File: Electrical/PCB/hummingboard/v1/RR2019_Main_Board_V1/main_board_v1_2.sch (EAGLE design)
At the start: 143 parts, among them CN1 MIRCO_B, IC1 OR_SC70-5, J10 I2C_5V_4, J11 SERVO_LEFT, J12 SERVO_RIGHT, J13 ESC, J14 5V_INPUT, J15 QUAD_ENCODER_2, J16 7.2V_INPUT, J17 I2C_5V_FXIO_1, J18 I2C_5V_FXIO_2, J19 JETSON_TRIGGER, J2 REAR_ENCODER, J20 QUAD_ENCODER_1, J21 BLDC_HALL, J22 SPI_FXIO_1, J3 FRONT_ENCODER, J4 I2C_1V8_1, J5 SPI_2, J6 WIRELESS_MODULE, J7 UART_0, J8 UART_2, J9 STEERING_ANGLE, Q1 BSS138, Q3 DMP2066LSN, Q4 BSS138, Q5 BSS138, Q6 BSS138, Q7 BSS138, Q8 BSS138, U3 ICM-20948, U4 PCA9306

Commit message: layout complete v.1
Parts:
- added JP12: POWER2, adafruit:PINHD-1X3
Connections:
- net +1.8V: now also JP6.4; no longer JP6.5
- net +3V3: now also JP12.1, JP12.2; no longer JP6.4
- net GND: now also JP12.3, JP6.5
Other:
- moved on the sheet: JP6
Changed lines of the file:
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@@
 <part name="U$46" library="RobotRacing2019_Master" deviceset="+VDD" device=""/>
 <part name="JP6" library="adafruit" library_urn="urn:adsk.eagle:library:420" deviceset="PINHD-1X8" device="BIG" package3d_urn="urn:adsk.eagle:package:6240707/1" value="POWER"/>
-<part name="U$47" library="RobotRacing2019_Master" deviceset="+3V3" device=""/>
 <part name="JP7" library="adafruit" library_urn="urn:adsk.eagle:library:420" deviceset="PINHD-1X3" device="" package3d_urn="urn:adsk.eagle:package:6240710/1" value="ADC_1"/>
 <part name="JP9" library="adafruit" library_urn="urn:adsk.eagle:library:420" deviceset="PINHD-1X8" device="BIG" package3d_urn="urn:adsk.eagle:package:6240707/1" value="ADC_2"/>
@@
 <part name="S3" library="RobotRacing2019_Master" deviceset="M9040P" device="" package3d_urn="urn:adsk.eagle:package:27676/1" value="ON/OFF"/>
 <part name="DEBUD/RACE" library="special" library_urn="urn:adsk.eagle:library:367" deviceset="SW_DIP-1" device="" package3d_urn="urn:adsk.eagle:package:26661/1"/>
+<part name="JP12" library="adafruit" library_urn="urn:adsk.eagle:library:420" deviceset="PINHD-1X3" device="" package3d_urn="urn:adsk.eagle:package:6240710/1" value="POWER2"/>
+<part name="SUPPLY16" library="RobotRacing2019_Master" deviceset="GND" device=""/>
+<part name="U$40" library="RobotRacing2019_Master" deviceset="+3V3" device=""/>
 </parts>
 <sheets>
@@
 <attribute name="VALUE" x="52.07" y="-116.84" size="1.778" layer="96"/>
 </instance>
-<instance part="SUPPLY56" gate="GND" x="0" y="78.74" smashed="yes">
-<attribute name="VALUE" x="-1.905" y="75.565" size="1.778" layer="96"/>
+<instance part="SUPPLY56" gate="GND" x="-25.4" y="78.74" smashed="yes">
+<attribute name="VALUE" x="-27.305" y="75.565" size="1.778" layer="96"/>
 </instance>
-<instance part="U$46" gate="G$1" x="0" y="114.3" smashed="yes">
-<attribute name="VALUE" x="-1.524" y="115.316" size="1.27" layer="96"/>
+<instance part="U$46" gate="G$1" x="-25.4" y="114.3" smashed="yes">
+<attribute name="VALUE" x="-26.924" y="115.316" size="1.27" layer="96"/>
 </instance>
-<instance part="JP6" gate="G$1" x="20.32" y="96.52" smashed="yes">
-<attribute name="NAME" x="13.97" y="107.315" size="1.778" layer="95"/>
-<attribute name="VALUE" x="13.97" y="81.28" size="1.778" layer="96"/>
-</instance>
-<instance part="U$47" gate="G$1" x="-7.62" y="111.76" smashed="yes">
-<attribute name="VALUE" x="-9.144" y="115.316" size="1.27" layer="96"/>
+<instance part="JP6" gate="G$1" x="-5.08" y="96.52" smashed="yes">
+<attribute name="NAME" x="-11.43" y="107.315" size="1.778" layer="95"/>
+<attribute name="VALUE" x="-11.43" y="81.28" size="1.778" layer="96"/>
 </instance>
 <instance part="JP7" gate="A" x="40.64" y="-160.02" smashed="yes">
@@
 <attribute name="VALUE" x="28.575" y="-333.375" size="1.778" layer="96"/>
 </instance>
-<instance part="U$29" gate="G$1" x="-15.24" y="111.76" smashed="yes"/>
+<instance part="U$29" gate="G$1" x="-30.48" y="111.76" smashed="yes"/>
+<instance part="JP12" gate="A" x="33.02" y="96.52" smashed="yes">
+<attribute name="NAME" x="26.67" y="102.235" size="1.778" layer="95"/>
+<attribute name="VALUE" x="26.67" y="88.9" size="1.778" layer="96"/>
+</instance>
+<instance part="SUPPLY16" gate="GND" x="20.32" y="83.82" smashed="yes">
+<attribute name="VALUE" x="18.415" y="80.645" size="1.778" layer="96"/>
+</instance>
+<instance part="U$40" gate="G$1" x="20.32" y="109.22" smashed="yes"/>
 </instances>
 <busses>
@@
 <pinref part="SUPPLY56" gate="GND" pin="GND"/>
 <pinref part="JP6" gate="G$1" pin="7"/>
-<wire x1="0" y1="88.9" x2="0" y2="86.36" width="0.1524" layer="91"/>
-<wire x1="0" y1="86.36" x2="0" y2="81.28" width="0.1524" layer="91"/>
-<wire x1="17.78" y1="88.9" x2="0" y2="88.9" width="0.1524" layer="91"/>
+<wire x1="-25.4" y1="88.9" x2="-25.4" y2="86.36" width="0.1524" layer="91"/>
+<wire x1="-25.4" y1="86.36" x2="-25.4" y2="81.28" width="0.1524" layer="91"/>
+<wire x1="-7.62" y1="88.9" x2="-25.4" y2="88.9" width="0.1524" layer="91"/>
 <pinref part="JP6" gate="G$1" pin="8"/>
-<wire x1="17.78" y1="86.36" x2="0" y2="86.36" width="0.1524" layer="91"/>
-<junction x="0" y="86.36"/>
+<wire x1="-7.62" y1="86.36" x2="-25.4" y2="86.36" width="0.1524" layer="91"/>
+<junction x="-25.4" y="86.36"/>
 <pinref part="JP6" gate="G$1" pin="6"/>
-<wire x1="17.78" y1="91.44" x2="0" y2="91.44" width="0.1524" layer="91"/>
-<wire x1="0" y1="91.44" x2="0" y2="88.9" width="0.1524" layer="91"/>
-<junction x="0" y="88.9"/>
+<wire x1="-7.62" y1="91.44" x2="-25.4" y2="91.44" width="0.1524" layer="91"/>
+<wire x1="-25.4" y1="91.44" x2="-25.4" y2="88.9" width="0.1524" layer="91"/>
+<junction x="-25.4" y="88.9"/>
+<pinref part="JP6" gate="G$1" pin="5"/>
+<wire x1="-7.62" y1="93.98" x2="-25.4" y2="93.98" width="0.1524" layer="91"/>
+<wire x1="-25.4" y1="93.98" x2="-25.4" y2="91.44" width="0.1524" layer="91"/>
+<junction x="-25.4" y="91.44"/>
 </segment>
 <segment>
@@
 <wire x1="30.48" y1="-325.12" x2="30.48" y2="-327.66" width="0.1524" layer="91"/>
 </segment>
+<segment>
+<pinref part="JP12" gate="A" pin="3"/>
+<wire x1="30.48" y1="93.98" x2="20.32" y2="93.98" width="0.1524" layer="91"/>
+<wire x1="20.32" y1="93.98" x2="20.32" y2="86.36" width="0.1524" layer="91"/>
+<pinref part="SUPPLY16" gate="GND" pin="GND"/>
+</segment>
 </net>
 <net name="ADC1_SE6_/_ACMP1_IN6_/_FTM0_FLT3" class="0">
@@
 <net name="+VDD" class="0">
 <segment>
-<wire x1="17.78" y1="101.6" x2="0" y2="101.6" width="0.1524" layer="91"/>
-<wire x1="17.78" y1="104.14" x2="0" y2="104.14" width="0.1524" layer="91"/>
-<label x="2.54" y="106.68" size="1.778" layer="95"/>
-<wire x1="0" y1="101.6" x2="0" y2="104.14" width="0.1524" layer="91"/>
-<wire x1="0" y1="104.14" x2="0" y2="111.76" width="0.1524" layer="91"/>
-<junction x="0" y="104.14"/>
+<wire x1="-7.62" y1="101.6" x2="-25.4" y2="101.6" width="0.1524" layer="91"/>
+<wire x1="-7.62" y1="104.14" x2="-25.4" y2="104.14" width="0.1524" layer="91"/>
+<label x="-22.86" y="106.68" size="1.778" layer="95"/>
+<wire x1="-25.4" y1="101.6" x2="-25.4" y2="104.14" width="0.1524" layer="91"/>
+<wire x1="-25.4" y1="104.14" x2="-25.4" y2="111.76" width="0.1524" layer="91"/>
+<junction x="-25.4" y="104.14"/>
 <pinref part="U$46" gate="G$1" pin="+VDD"/>
 <pinref part="JP6" gate="G$1" pin="1"/>
 <pinref part="JP6" gate="G$1" pin="2"/>
 <pinref part="JP6" gate="G$1" pin="3"/>
-<wire x1="17.78" y1="99.06" x2="0" y2="99.06" width="0.1524" layer="91"/>
-<wire x1="0" y1="99.06" x2="0" y2="101.6" width="0.1524" layer="91"/>
-<junction x="0" y="101.6"/>
+<wire x1="-7.62" y1="99.06" x2="-25.4" y2="99.06" width="0.1524" layer="91"/>
+<wire x1="-25.4" y1="99.06" x2="-25.4" y2="101.6" width="0.1524" layer="91"/>
+<junction x="-25.4" y="101.6"/>
 </segment>
 </net>
-<net name="+3V3" class="0">
+<net name="+1.8V" class="0">
 <segment>
-<wire x1="17.78" y1="96.52" x2="-7.62" y2="96.52" width="0.1524" layer="91"/>
+<pinref part="U$29" gate="G$1" pin="+1.8V"/>
 <pinref part="JP6" gate="G$1" pin="4"/>
-<label x="-2.54" y="96.52" size="1.778" layer="95"/>
-<wire x1="-7.62" y1="96.52" x2="-7.62" y2="111.76" width="0.1524" layer="91"/>
-<pinref part="U$47" gate="G$1" pin="+3V3"/>
+<wire x1="-30.48" y1="96.52" x2="-30.48" y2="111.76" width="0.1524" layer="91"/>
+<wire x1="-7.62" y1="96.52" x2="-30.48" y2="96.52" width="0.1524" layer="91"/>
 </segment>
 </net>
-<net name="+1.8V" class="0">
+<net name="+3V3" class="0">
 <segment>
-<pinref part="JP6" gate="G$1" pin="5"/>
-<wire x1="17.78" y1="93.98" x2="-15.24" y2="93.98" width="0.1524" layer="91"/>
-<wire x1="-15.24" y1="93.98" x2="-15.24" y2="111.76" width="0.1524" layer="91"/>
-<pinref part="U$29" gate="G$1" pin="+1.8V"/>
+<pinref part="U$40" gate="G$1" pin="+3V3"/>
+<wire x1="20.32" y1="109.22" x2="20.32" y2="99.06" width="0.1524" layer="91"/>
+<pinref part="JP12" gate="A" pin="1"/>
+<wire x1="20.32" y1="99.06" x2="30.48" y2="99.06" width="0.1524" layer="91"/>
+<pinref part="JP12" gate="A" pin="2"/>
+<wire x1="30.48" y1="96.52" x2="20.32" y2="96.52" width="0.1524" layer="91"/>
+<wire x1="20.32" y1="96.52" x2="20.32" y2="99.06" width="0.1524" layer="91"/>
+<junction x="20.32" y="99.06"/>
 </segment>
 </net>

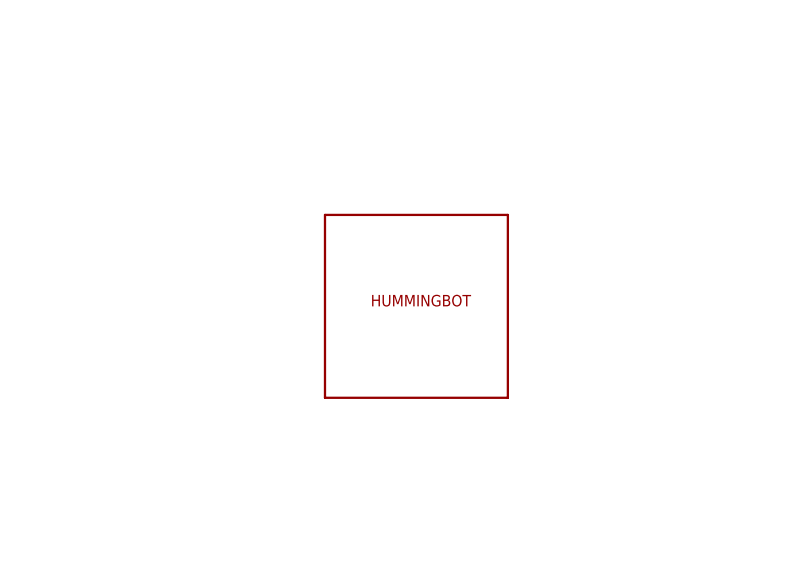
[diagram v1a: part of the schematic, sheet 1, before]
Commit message: layout and power planed modified, complete v2
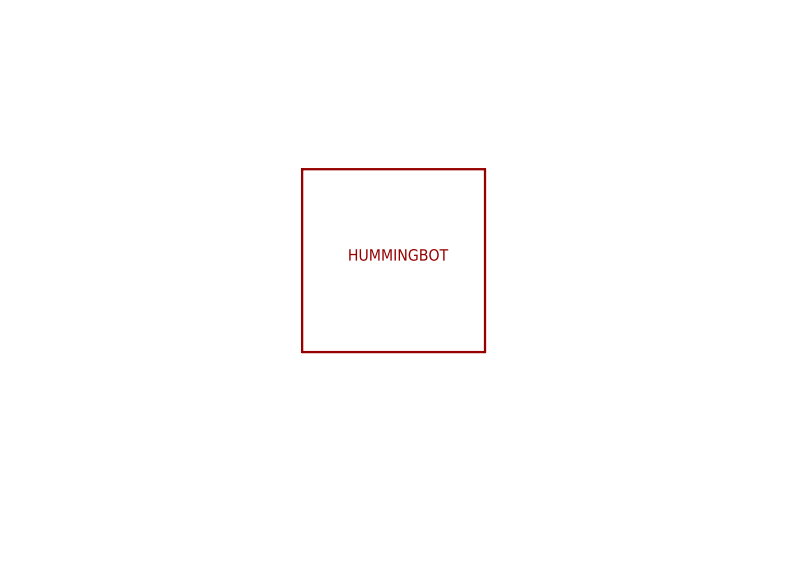
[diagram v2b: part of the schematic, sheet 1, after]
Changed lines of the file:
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@@
 <part name="SUPPLY47" library="RobotRacing2019_Master" deviceset="GND" device=""/>
 <part name="SUPPLY55" library="RobotRacing2019_Master" deviceset="GND" device=""/>
-<part name="U$44" library="RobotRacing2019_Master" deviceset="TEAM_LOGO" device=""/>
 <part name="J19" library="RobotRacing2019_Master" deviceset="PINHEAD-2-VERTICAL" device="" value="JETSON_TRIGGER"/>
 <part name="C24" library="RobotRacing2019_Master" deviceset="CAP0603" device="" value="0.1u"/>
@@
 <part name="SUPPLY16" library="RobotRacing2019_Master" deviceset="GND" device=""/>
 <part name="U$40" library="RobotRacing2019_Master" deviceset="+3V3" device=""/>
+<part name="U$44" library="RobotRacing2019_Master" deviceset="TEAM_LOGO" device=""/>
 </parts>
 <sheets>
@@
 <attribute name="VALUE" x="-189.484" y="13.716" size="1.27" layer="96"/>
 </instance>
-<instance part="U$44" gate="G$1" x="-172.72" y="104.14" smashed="yes"/>
 <instance part="U$34" gate="G$1" x="-259.08" y="119.38" smashed="yes"/>
 <instance part="RC/AUTO" gate="G$1" x="-325.12" y="-78.74" smashed="yes" rot="R270">
@@
 <attribute name="VALUE" x="-276.86" y="-73.66" size="1.778" layer="96" rot="R270"/>
 </instance>
+<instance part="U$44" gate="G$1" x="-175.26" y="109.22" smashed="yes"/>
 </instances>
 <busses>
